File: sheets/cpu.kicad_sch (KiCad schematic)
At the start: 6 parts, among them J1 BERR, U1 43256, U2 43256, U3 HD68HC000P, U4 NEO-C1

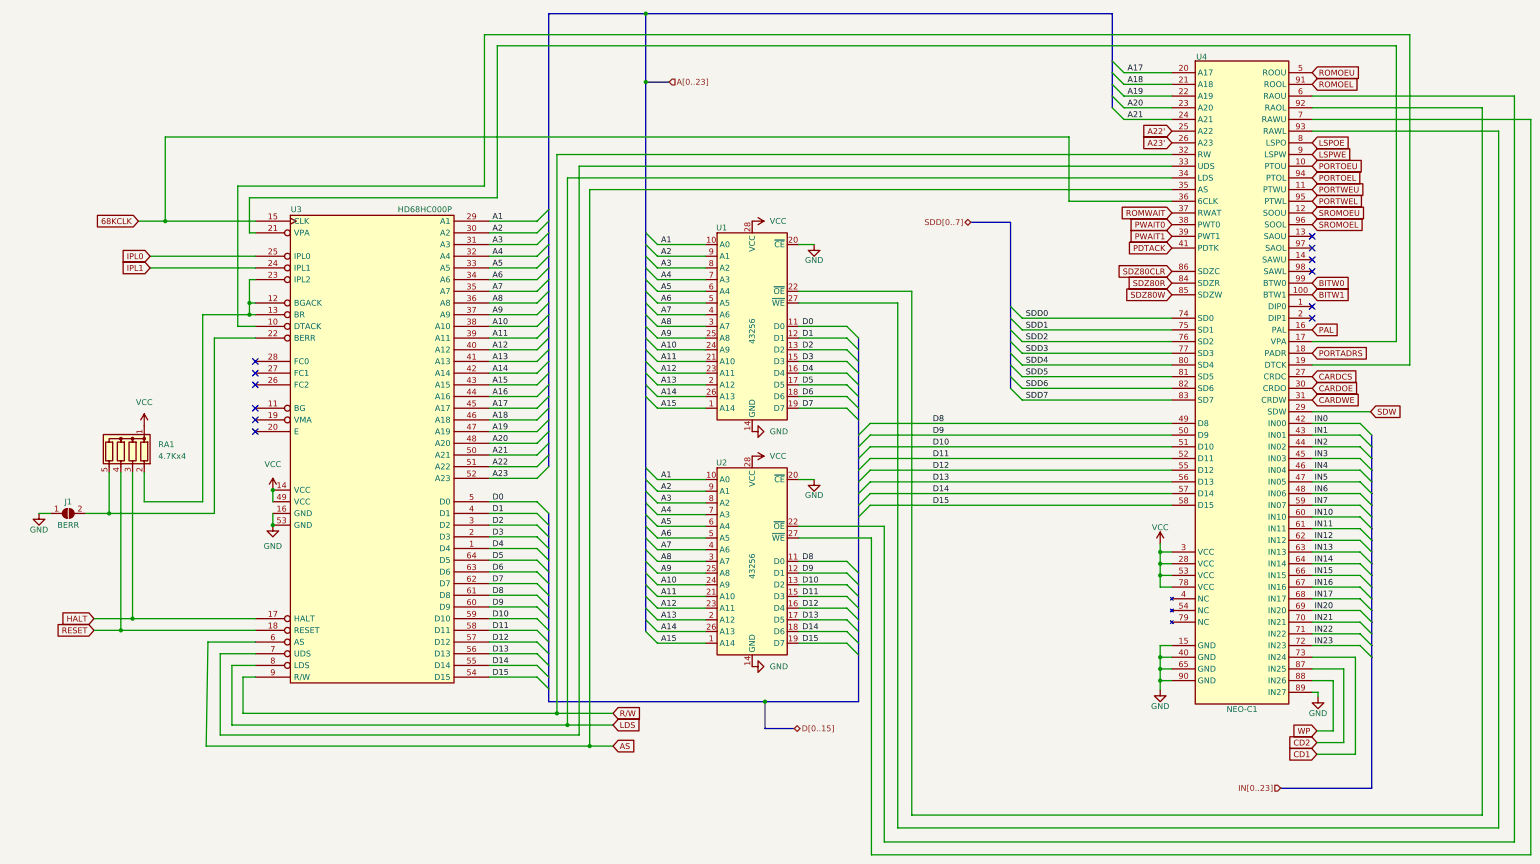
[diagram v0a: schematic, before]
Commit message: Updated to Kicad 10
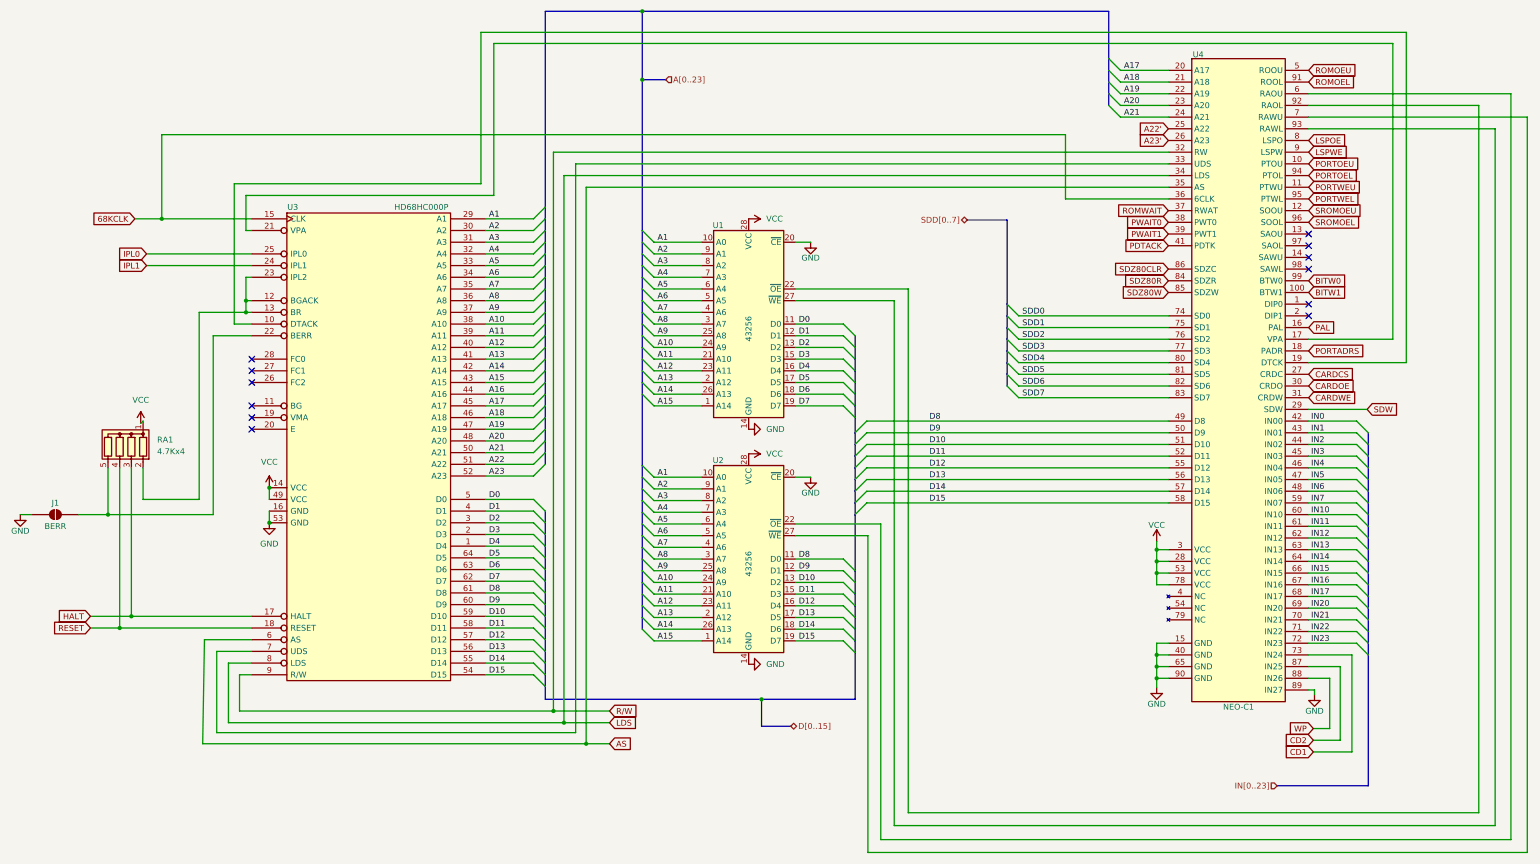
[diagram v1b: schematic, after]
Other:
- moved on the sheet: RA1, U1, U2, U3, U4
